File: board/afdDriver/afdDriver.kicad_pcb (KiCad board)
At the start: 2 copper layers, 43 parts, among them J1 SegmentEnables, J2 HighVoltageAC, U1 QTM3063T1, U2 QTM3063T1, U3 QTM3063T1, U4 QTM3063T1, U5 QTM3063T1, U6 QTM3063T1, U7 QTM3063T1, U8 QTM3063T1

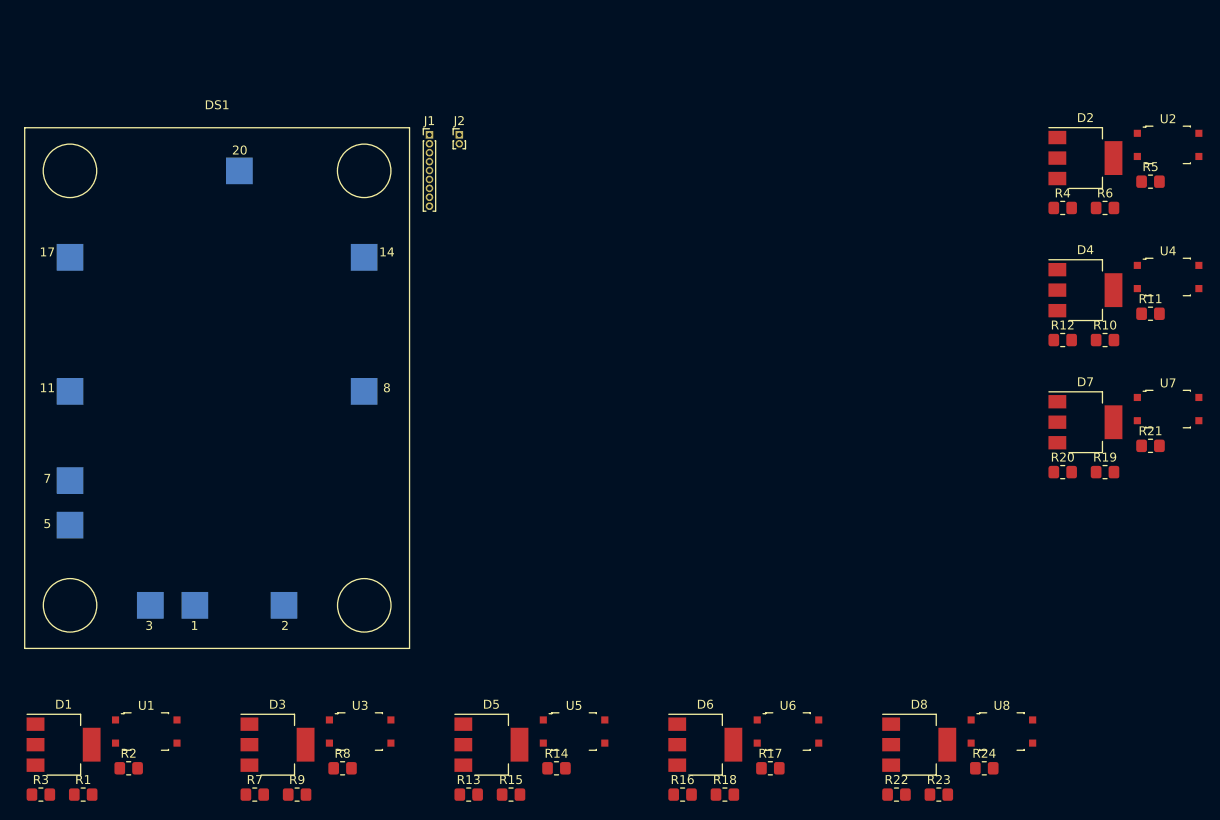
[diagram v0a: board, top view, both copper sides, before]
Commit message: Added two ground posts.
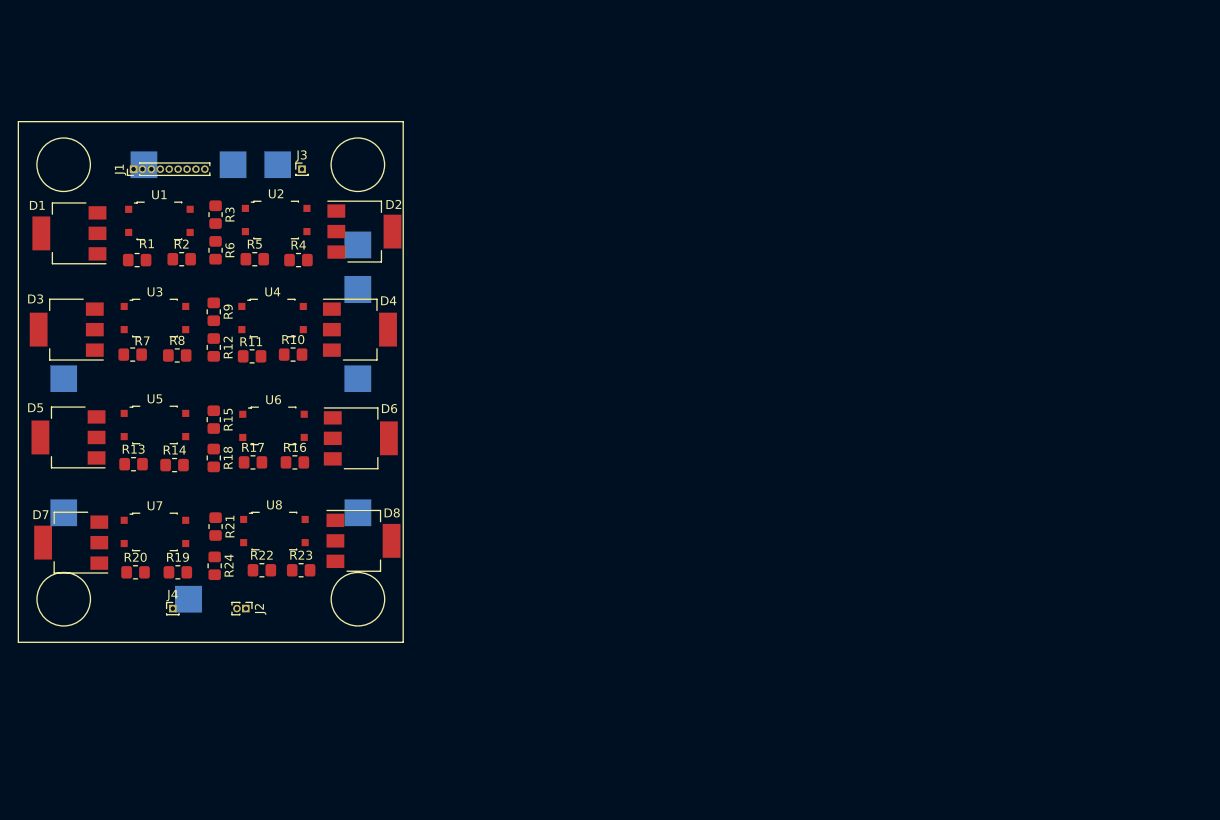
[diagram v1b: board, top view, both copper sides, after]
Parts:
- added J3: GND Pin #1, Connector_PinHeader_1.00mm:PinHeader_1x01_P1.00mm_Vertical, F.Cu at (109.3, 63.7)
- added J4: GND Pin #2, Connector_PinHeader_1.00mm:PinHeader_1x01_P1.00mm_Vertical, F.Cu at (94.8, 113.0)
- DS1: value IEL-O-VI_C63.396.208-02 -> IEL-O-VI_C63.396.208-02_SMD
- moved D7 114.6 mm to (83.4, 105.6), turned to 180 degrees
- moved U7 114.5 mm to (92.8, 104.4)
- moved R21 105.3 mm to (99.6, 103.8), turned to 270 degrees
- moved R19 104.6 mm to (95.4, 108.9)
- moved R20 104.6 mm to (90.6, 108.9)
- moved R11 100.9 mm to (103.7, 84.7), turned to 180 degrees
- moved R5 100.9 mm to (104.0, 73.8)
- moved U4 100.6 mm to (106.0, 80.4)
- moved U2 100.4 mm to (106.4, 69.4)
- moved R6 99.9 mm to (99.6, 72.8), turned to 270 degrees
- moved R12 95.3 mm to (99.4, 83.7), turned to 270 degrees
- moved R10 91.1 mm to (108.3, 84.5)
- moved R24 89.3 mm to (99.5, 108.2), turned to 270 degrees
- moved R4 85.9 mm to (108.9, 73.9)
- moved U8 84.7 mm to (106.2, 104.3)
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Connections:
- DS1 pad 5: (no net) -> Net-(DS1-Pad5)

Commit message: Checkpoint. Starting layout.
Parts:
- DS1: moved to B.Cu
- moved D7 48.4 mm to (117.6, 71.4), turned to 0 degrees
- moved R24 45.3 mm to (110.5, 64.3), turned to 0 degrees
- moved R22 44.8 mm to (101.6, 64.0), turned to 270 degrees
- moved U8 44.6 mm to (108.0, 59.7)
- moved R23 44.6 mm to (105.7, 64.3), turned to 180 degrees
- moved D8 44.5 mm to (117.6, 61.0)
- moved U7 37.5 mm to (108.0, 70.1)
- moved R20 37.4 mm to (105.7, 74.7), turned to 180 degrees
- moved R19 35.1 mm to (101.6, 74.3), turned to 270 degrees
- moved D5 34.5 mm to (117.6, 92.2), turned to 0 degrees
- moved D4 32.0 mm to (85.6, 92.3), turned to 180 degrees
- moved R21 31.1 mm to (110.5, 74.7), turned to 0 degrees
- moved D2 30.7 mm to (85.6, 71.5), turned to 180 degrees
- moved R1 18.5 mm to (101.6, 58.9), turned to 270 degrees
- moved R18 15.6 mm to (110.5, 85.1), turned to 0 degrees
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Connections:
- DS1 pad 5: Net-(DS1-Pad5) -> (no net)
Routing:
- net /EnbSegE: track 0.00 -> 89.3 mm
- net Net-(D1-Pad3): track 0.00 -> 79.8 mm
- net /SegE: track 0.00 -> 64.3 mm
- net /SegD: track 0.00 -> 57.9 mm
- net /SegA: track 0.00 -> 47.4 mm
- net /EnbSegD: track 0.00 -> 47.0 mm
- net /EnbSegC: track 0.00 -> 37.7 mm
- net /SegG: track 0.00 -> 37.4 mm
- net /EnbSegF: track 0.00 -> 31.0 mm
- net /SegB: track 0.00 -> 30.5 mm
- net /SegF: track 0.00 -> 27.1 mm
- net /EnbSegB: track 0.00 -> 26.0 mm
- net /SegH: track 0.00 -> 20.8 mm
- net /EnbSegG: track 0.00 -> 20.7 mm
- net /EnbSegA: track 0.00 -> 12.5 mm
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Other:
- board outline added: 43.2 x 58.4 mm
- copper layers 2 -> 4
- net class Default: clearance 0.2 -> 0.127; trace_width 0.25 -> 0.127; via_dia 0.8 -> 0.6; via_drill 0.4 -> 0.3
- rule trace_clearance: 0.2 -> 0.127
- rule trace_min: 0.2 -> 0.127
- rule via_min_size: 0.4 -> 0.6

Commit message: Checkpoint. New 3dmodels.
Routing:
- net GND1: track 0.00 -> 4.30 mm

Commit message: Updated.
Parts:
- removed the J3 at (110.7, 51.6)
- added C1: 0.1 uFd, Capacitor_SMD:C_0805_2012Metric_Pad1.18x1.45mm_HandSolder, F.Cu at (100.1, 54.4)
- added J2: Qwiic_Connector, Connector_JST:JST_SH_BM04B-SRSS-TB_1x04-1MP_P1.00mm_Vertical, F.Cu at (112.5, 101.1)
- added JP1: ADDR0, Jumper:SolderJumper-2_P1.3mm_Open_TrianglePad1.0x1.5mm, F.Cu at (100.6, 50.3)
- added JP2: ADDR1, Jumper:SolderJumper-2_P1.3mm_Open_TrianglePad1.0x1.5mm, F.Cu at (108.2, 50.3)
- added JP3: ADDR2, Jumper:SolderJumper-2_P1.3mm_Open_TrianglePad1.0x1.5mm, F.Cu at (112.5, 50.3)
- added R25: 390, Resistor_SMD:R_0805_2012Metric_Pad1.20x1.40mm_HandSolder, F.Cu at (92.9, 64.5)
- added R26: 390, Resistor_SMD:R_0805_2012Metric_Pad1.20x1.40mm_HandSolder, F.Cu at (101.9, 59.7)
- added R27: 390, Resistor_SMD:R_0805_2012Metric_Pad1.20x1.40mm_HandSolder, F.Cu at (97.7, 64.5)
- added U9: QTM3063T1, jdn_library:4-SMD_3.8x4.6mm, F.Cu at (95.0, 59.8)
- J1: value SegmentEnables -> Qwiic_Connector; footprint Connector_PinHeader_1.00mm:PinHeader_1x09_P1.00mm_Vertical -> Connector_JST:JST_SH_BM04B-SRSS-TB_1x04-1MP_P1.00mm_Vertical
- J4: value GND Pin #2 -> HighVoltageAC; footprint Connector_PinHeader_1.00mm:PinHeader_1x01_P1.00mm_Vertical -> Connector_PinHeader_1.00mm:PinHeader_1x02_P1.00mm_Vertical
- R1, R2, R3: value 390 -> 10K Ohm
- U1: value QTM3063T1 -> PCF8574TS; footprint jdn_library:4-SMD_3.8x4.6mm -> Package_SO:SSOP-20_4.4x6.5mm_P0.65mm
- moved J1 49.5 mm to (90.9, 101.1), turned to 270 degrees
- moved R3 21.5 mm to (112.5, 54.9)
- moved R2 13.8 mm to (108.2, 54.9)
- moved J4 13.7 mm to (103.6, 103.1), turned to 90 degrees
- moved U1 7.47 mm to (94.2, 52.3), turned to 90 degrees
- moved R1 4.79 mm to (104.1, 54.9), turned to 0 degrees
- moved J3 1.70 mm to (103.6, 99.1), turned to 90 degrees
- moved R11 0.51 mm to (93.2, 96.0)
- moved R12 0.51 mm to (98.0, 96.0)
- moved R14 0.51 mm to (105.7, 96.0)
- moved R15 0.51 mm to (110.5, 96.0)
- moved R17 0.51 mm to (105.7, 85.6)
- moved R18 0.51 mm to (110.5, 85.6)
- moved R20 0.51 mm to (105.7, 75.2)
- moved R21 0.51 mm to (110.5, 75.2)
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- renumbered J2 to J3
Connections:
- J1 pad 1: /EnbSegA -> GND
- J1 pad 2: /EnbSegB -> +3V3
- J1 pad 3: /EnbSegC -> /SDA
- J1 pad 4: /EnbSegD -> /SCL
- J4 pad 1: GND -> GND1
- R1 pad 1: Net-(R1-Pad1) -> +3V3
- R1 pad 2: GND -> /A0
- R12 pad 1: /SegD -> /SegC
- R12 pad 2: Net-(D4-Pad3) -> Net-(D3-Pad3)
- R15 pad 1: /SegE -> /SegD
- R15 pad 2: Net-(D5-Pad3) -> Net-(D4-Pad3)
- R18 pad 1: /SegF -> /SegE
- R18 pad 2: Net-(D6-Pad3) -> Net-(D5-Pad3)
- R2 pad 1: HV_AC -> +3V3
- R2 pad 2: Net-(R2-Pad2) -> /A1
- R21 pad 1: /SegG -> /SegF
- R21 pad 2: Net-(D7-Pad3) -> Net-(D6-Pad3)
- R24 pad 1: /SegH -> /SegG
- R24 pad 2: Net-(D8-Pad3) -> Net-(D7-Pad3)
- R3 pad 1: /SegA -> +3V3
- R3 pad 2: Net-(D1-Pad3) -> /A2
- R6 pad 1: /SegB -> /SegA
- R6 pad 2: Net-(D2-Pad3) -> Net-(D1-Pad3)
- R9 pad 1: /SegC -> /SegB
- R9 pad 2: Net-(D3-Pad3) -> Net-(D2-Pad3)
- U1 pad 1: /EnbSegA -> (no net)
- U1 pad 2: Net-(R1-Pad1) -> /SCL
- U1 pad 3: Net-(D1-Pad3) -> (no net)
- U1 pad 4: Net-(R2-Pad2) -> /SDA
- U2 pad 1: /EnbSegB -> /EnbSegA
- U2 pad 3: Net-(D2-Pad3) -> Net-(D1-Pad3)
- U3 pad 1: /EnbSegC -> /EnbSegB
- U3 pad 3: Net-(D3-Pad3) -> Net-(D2-Pad3)
- U4 pad 1: /EnbSegD -> /EnbSegC
- U4 pad 3: Net-(D4-Pad3) -> Net-(D3-Pad3)
- U5 pad 1: /EnbSegE -> /EnbSegD
- U5 pad 3: Net-(D5-Pad3) -> Net-(D4-Pad3)
- U6 pad 1: /EnbSegF -> /EnbSegE
- U6 pad 3: Net-(D6-Pad3) -> Net-(D5-Pad3)
- U7 pad 1: /EnbSegG -> /EnbSegF
- U7 pad 3: Net-(D7-Pad3) -> Net-(D6-Pad3)
- U8 pad 1: /EnbSegH -> /EnbSegG
- U8 pad 3: Net-(D8-Pad3) -> Net-(D7-Pad3)
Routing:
- net /EnbSegE: track 89.3 -> 0.00 mm
- net Net-(D1-Pad3): track 79.8 -> 0.00 mm
- net /SegE: track 64.3 -> 0.00 mm
- net /SegD: track 57.9 -> 0.00 mm
- net /SegA: track 47.4 -> 0.00 mm
- net /EnbSegD: track 47.0 -> 0.00 mm
- net /EnbSegC: track 37.7 -> 0.00 mm
- net /SegG: track 37.4 -> 0.00 mm
- net /EnbSegF: track 31.0 -> 0.00 mm
- net /SegB: track 30.5 -> 0.00 mm
- net /SegF: track 27.1 -> 0.00 mm
- net /EnbSegB: track 26.0 -> 0.00 mm
- net /SegH: track 20.8 -> 0.00 mm
- net /EnbSegG: track 20.7 -> 0.00 mm
- net /EnbSegA: track 12.5 -> 0.00 mm
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- added copper zone on B.Cu, net GND
- added copper zone on F.Cu, net HV_AC

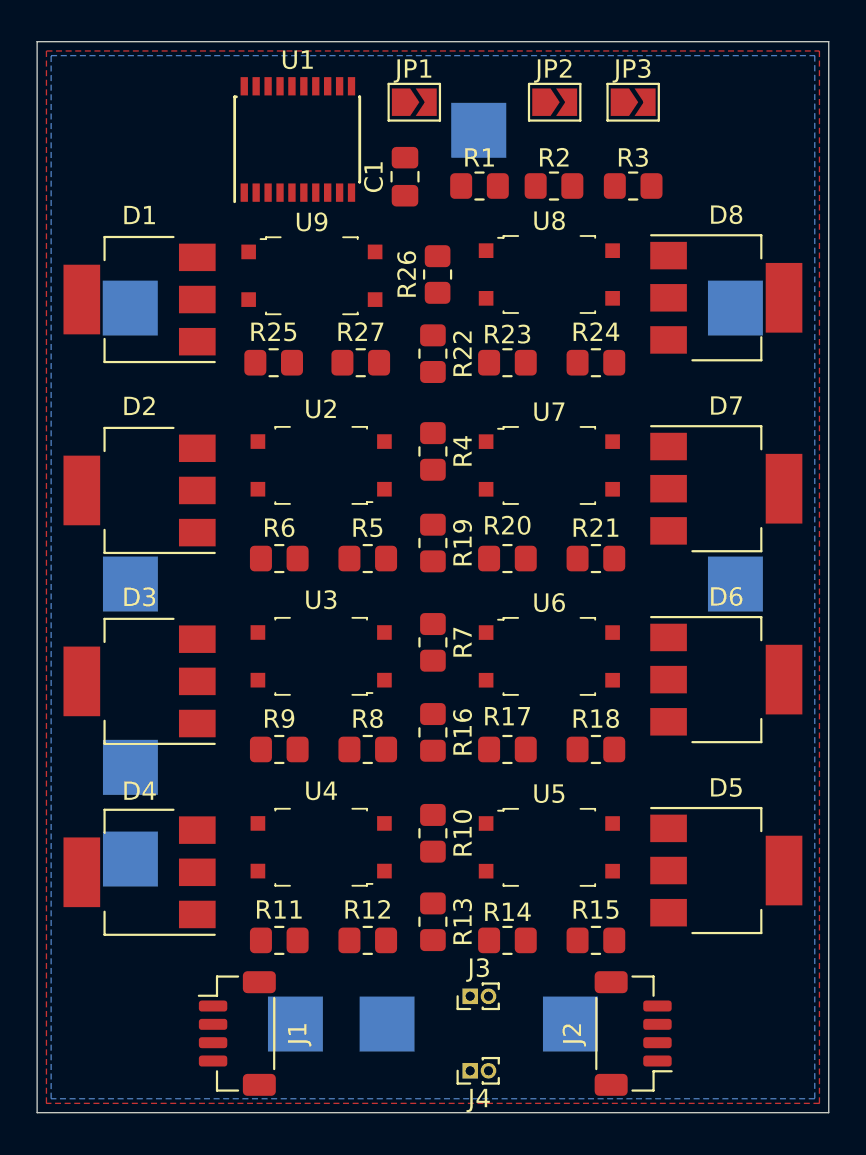
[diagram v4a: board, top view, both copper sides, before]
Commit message: Auto-routed.
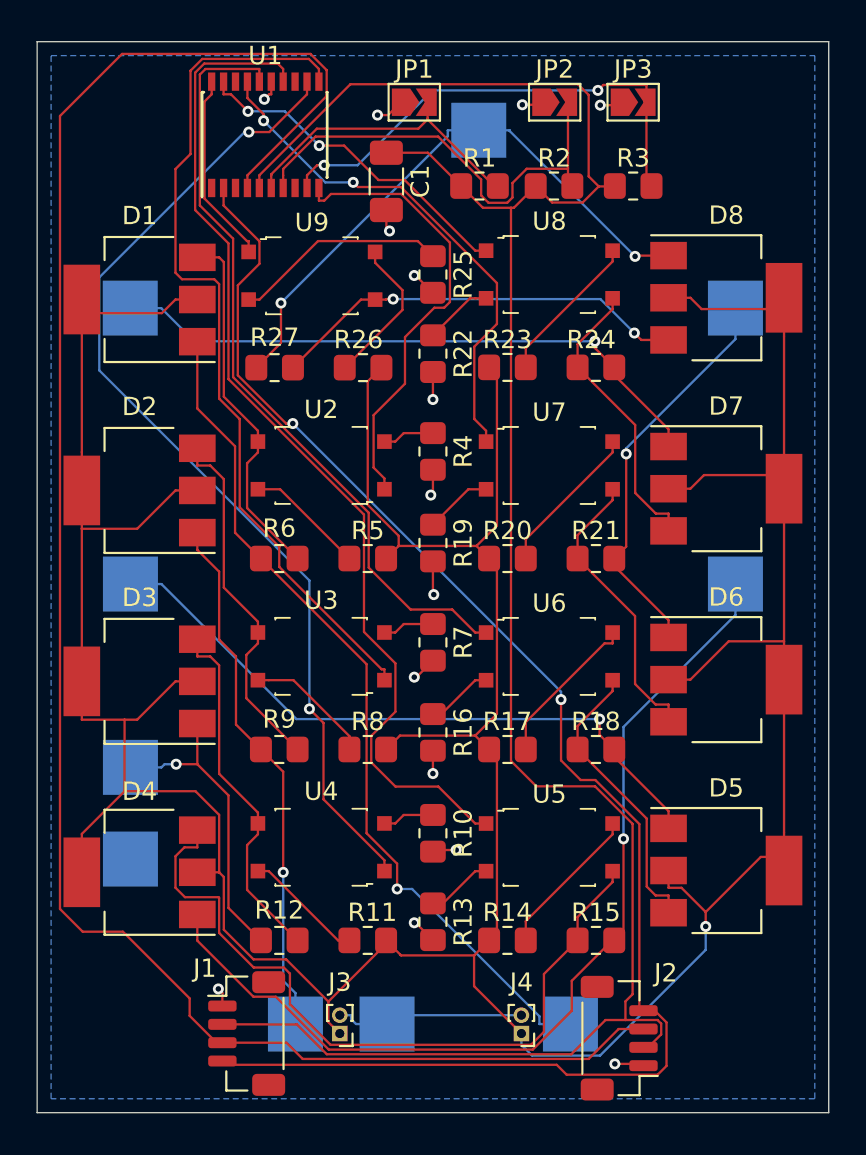
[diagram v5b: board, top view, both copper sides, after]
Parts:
- C1: footprint Capacitor_SMD:C_0805_2012Metric_Pad1.18x1.45mm_HandSolder -> Capacitor_SMD:C_1206_3216Metric_Pad1.33x1.80mm_HandSolder
- moved R25 9.93 mm to (101.6, 59.7), turned to 270 degrees
- moved J3 7.40 mm to (96.5, 101.1), turned to 180 degrees
- moved R26 6.51 mm to (97.8, 64.8), turned to 180 degrees
- moved R11 4.83 mm to (98.0, 96.0), turned to 180 degrees
- moved R12 4.83 mm to (93.2, 96.0)
- moved R27 4.71 mm to (93.0, 64.8)
- moved J4 3.45 mm to (106.4, 101.1), turned to 180 degrees
- moved U1 1.80 mm to (92.5, 52.1)
- moved C1 1.05 mm to (99.1, 54.6), turned to 270 degrees
- moved J2 0.80 mm to (111.8, 101.3)
- moved J1 0.51 mm to (91.4, 101.1)
- moved R23 0.25 mm to (105.7, 64.8), turned to 0 degrees
- moved R24 0.25 mm to (110.5, 64.8), turned to 180 degrees
- turned R14 to 0 degrees
- turned R15 to 180 degrees
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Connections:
- J4 pad 1: GND1 -> HV_AC
- J4 pad 2: HV_AC -> GND1
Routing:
- net HV_AC: track 0.00 -> 222.6 mm, vias 0 -> 1
- net +3V3: track 0.00 -> 117.5 mm
- net /SDA: track 0.00 -> 104.2 mm
- net /SCL: track 0.00 -> 84.7 mm, vias 0 -> 2
- net /EnbSegD: track 0.00 -> 56.2 mm
- net /EnbSegC: track 0.00 -> 55.0 mm, vias 0 -> 2
- net /SegD: track 0.00 -> 52.2 mm, vias 0 -> 1
- net /EnbSegB: track 0.00 -> 47.6 mm
- net /SegA: track 0.00 -> 47.1 mm, vias 0 -> 1
- net /EnbSegE: track 0.00 -> 42.6 mm
- net Net-(D4-Pad3): track 0.00 -> 40.4 mm
- net /SegE: track 0.00 -> 36.2 mm, vias 0 -> 1
- net /SegG: track 0.00 -> 33.5 mm, vias 0 -> 1
- net /SegH: track 0.00 -> 32.2 mm, vias 0 -> 2
- net /SegB: track 0.00 -> 29.0 mm, vias 0 -> 1
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- added copper zone on In1.Cu, net GND
- added copper zone on In2.Cu, net GND1
- removed copper zone on F.Cu, net HV_AC

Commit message: V1.0.0 design.
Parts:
- added H1: MountingHole, MountingHole:MountingHole_4.3mm_M4_ISO14580, F.Cu at (85.0, 52.0)
- added H2: MountingHole, MountingHole:MountingHole_4.3mm_M4_ISO14580, F.Cu at (118.2, 52.0)
- added H3: MountingHole, MountingHole:MountingHole_4.3mm_M4_ISO14580, F.Cu at (118.2, 100.4)
- added H4: MountingHole, MountingHole:MountingHole_4.3mm_M4_ISO14580, F.Cu at (85.0, 100.4)
- added J5: Power, Connector_PinSocket_2.54mm:PinSocket_1x02_P2.54mm_Vertical, F.Cu at (102.6, 99.3)
- J3, J4: footprint Connector_PinHeader_1.00mm:PinHeader_1x02_P1.00mm_Vertical -> Connector_PinSocket_2.54mm:PinSocket_1x02_P2.54mm_Vertical
- moved D1 45.2 mm to (117.9, 92.7), turned to 0 degrees
- moved D5 38.4 mm to (85.3, 71.4), turned to 180 degrees
- moved D7 34.0 mm to (85.3, 60.7), turned to 180 degrees
- moved D4 33.8 mm to (117.9, 82.3), turned to 0 degrees
- moved R4 28.4 mm to (110.7, 96.3), turned to 180 degrees
- moved U2 24.6 mm to (108.2, 91.2)
- moved R6 24.5 mm to (105.7, 96.3), turned to 180 degrees
- moved D2 21.0 mm to (85.3, 92.5)
- moved R5 20.6 mm to (101.6, 95.5), turned to 90 degrees
- moved R7 18.9 mm to (92.5, 96.3), turned to 0 degrees
- moved R18 16.8 mm to (97.5, 74.9), turned to 0 degrees
- moved U6 16.8 mm to (95.0, 69.8)
- moved R17 16.8 mm to (101.6, 69.3), turned to 90 degrees
- moved R11 16.1 mm to (101.6, 80.3), turned to 90 degrees
- moved R16 13.3 mm to (92.5, 74.9), turned to 0 degrees
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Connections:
- C1 pad 1: +3V3 -> +5V
- J1 pad 2: +3V3 -> +5V
- J2 pad 2: +3V3 -> +5V
- R1 pad 1: +3V3 -> +5V
- R10 pad 2: GND -> /EnbSegC
- R13 pad 2: GND -> /EnbSegD
- R16 pad 2: GND -> /EnbSegE
- R19 pad 2: GND -> /EnbSegF
- R2 pad 1: +3V3 -> +5V
- R22 pad 2: GND -> /EnbSegG
- R25 pad 2: GND -> /EnbSegH
- R3 pad 1: +3V3 -> +5V
- R4 pad 2: GND -> /EnbSegA
- R7 pad 2: GND -> /EnbSegB
- U1 pad 5: +3V3 -> +5V
- U2 pad 1: /EnbSegA -> +5V
- U3 pad 1: /EnbSegB -> +5V
- U4 pad 1: /EnbSegC -> +5V
- U5 pad 1: /EnbSegD -> +5V
- U6 pad 1: /EnbSegE -> +5V
- U7 pad 1: /EnbSegF -> +5V
- U8 pad 1: /EnbSegG -> +5V
- U9 pad 1: /EnbSegH -> +5V
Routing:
- net +5V: track 0.00 -> 201.3 mm, vias 0 -> 1
- net +3V3: track 117.5 -> 0.00 mm
- net /EnbSegA: track 24.8 -> 60.5 mm
- net /SegD: track 52.2 -> 18.7 mm
- net /EnbSegB: track 47.6 -> 73.9 mm
- net /SegA: track 47.1 -> 21.8 mm
- net /SCL: track 84.7 -> 109.5 mm, vias 2 -> 0
- net /SegE: track 36.2 -> 14.4 mm
- net Net-(D4-Pad3): track 40.4 -> 19.4 mm
- net /SegG: track 33.5 -> 15.2 mm
- net /EnbSegC: track 55.0 -> 37.7 mm
- net /EnbSegH: track 10.5 -> 27.7 mm, vias 0 -> 2
- net /SegB: track 29.0 -> 13.4 mm
- net /EnbSegD: track 56.2 -> 43.4 mm, vias 0 -> 2
- net GND: track 20.3 -> 8.49 mm, vias 15 -> 8
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- removed copper zone on In1.Cu, net GND
- removed copper zone on In2.Cu, net GND1
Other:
- copper layers 4 -> 2
